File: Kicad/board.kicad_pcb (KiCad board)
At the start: 2 copper layers, 100 x 91.4 mm, 28 parts, among them SW1 SW_Push, SW10 SW_Push, SW11 SW_Push, SW12 SW_Push, SW13 RotaryEncoder, SW2 SW_Push, SW3 SW_Push, SW4 SW_Push, SW5 SW_Push, SW6 SW_Push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

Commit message: [add] add through hole
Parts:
- added H1: MountingHole, MountingHole:MountingHole_2.7mm, F.Cu at (62.9, 36.6)
- added H2: MountingHole, MountingHole:MountingHole_2.7mm, F.Cu at (154.9, 36.6)
- added H3: MountingHole, MountingHole:MountingHole_2.7mm, F.Cu at (62.9, 120.0)
- added H4: MountingHole, MountingHole:MountingHole_2.7mm, F.Cu at (154.9, 120.0)
- D1, D10, D11, D12, D2, D3, D4, D5, D6, D7, D8, D9: footprint Diode_SMD:D_SOD-323 -> mylib:1n4148ws_reversible
- moved U2 34.0 mm to (98.0, 107.7)
- moved U3 34.0 mm to (101.3, 122.0)
- moved SW13 21.7 mm to (145.9, 117.2)
- moved D2 14.2 mm to (94.3, 37.6)
- moved D1 14.2 mm to (75.3, 37.6)
- moved D3 14.2 mm to (113.4, 37.6)
- moved D4 14.2 mm to (132.4, 37.6)
- moved U1 3.03 mm to (146.7, 51.6)
- moved D5 2.37 mm to (64.9, 57.3)
- moved D6 2.37 mm to (82.9, 57.3)
- moved D7 2.37 mm to (100.9, 57.3)
- moved D8 2.37 mm to (118.9, 57.3)
- moved D10 2.32 mm to (83.7, 77.7)
- moved D11 2.32 mm to (100.7, 77.7)
- moved D12 2.32 mm to (117.7, 77.7)
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
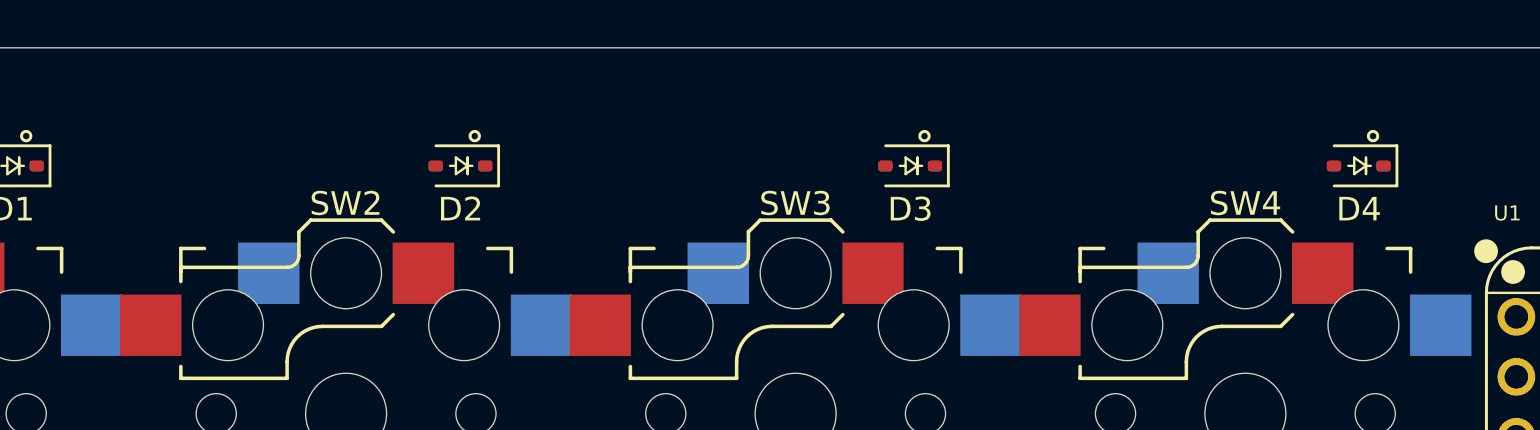
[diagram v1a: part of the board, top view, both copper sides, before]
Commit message: [update] move diodes
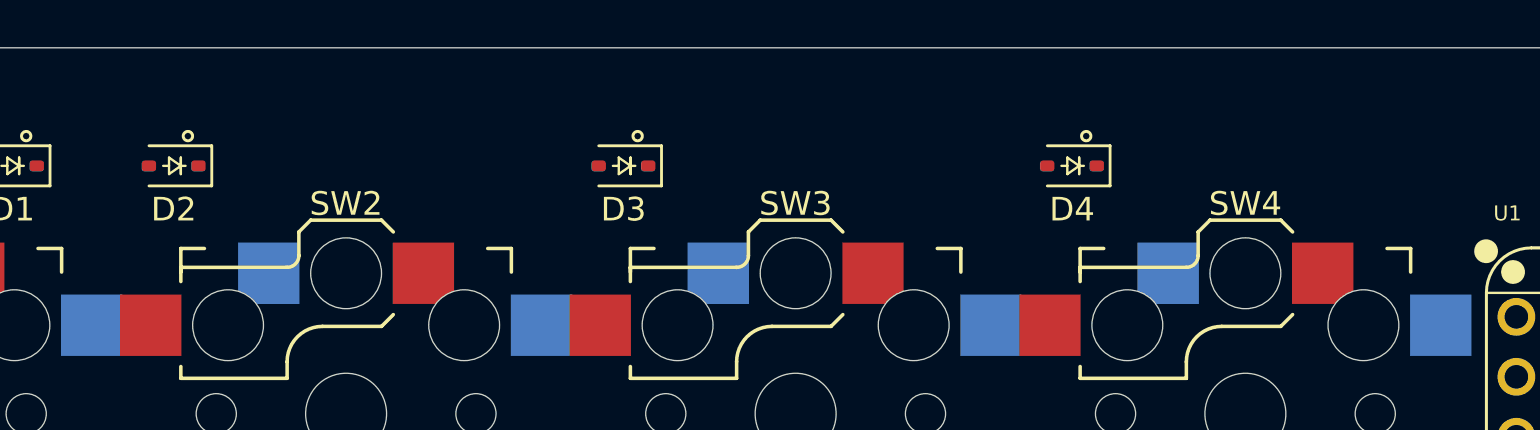
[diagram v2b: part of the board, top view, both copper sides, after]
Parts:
- moved D2 12.2 mm to (82.2, 37.6)
- moved D3 12.2 mm to (101.2, 37.6)
- moved D4 12.1 mm to (120.2, 37.6)
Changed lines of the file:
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@@
 	(footprint "mylib:1n4148ws_reversible"
 		(layer "F.Cu")
-		(at 113.3875 37.625 180)
+		(at 101.2375 37.625 180)
 		(descr "SOD-323")
 		(tags "SOD-323")
@@
 	(footprint "mylib:1n4148ws_reversible"
 		(layer "F.Cu")
-		(at 132.3875 37.625 180)
+		(at 120.2375 37.625 180)
 		(descr "SOD-323")
 		(tags "SOD-323")
@@
 	(footprint "mylib:1n4148ws_reversible"
 		(layer "F.Cu")
-		(at 94.3375 37.625 180)
+		(at 82.1875 37.625 180)
 		(descr "SOD-323")
 		(tags "SOD-323")

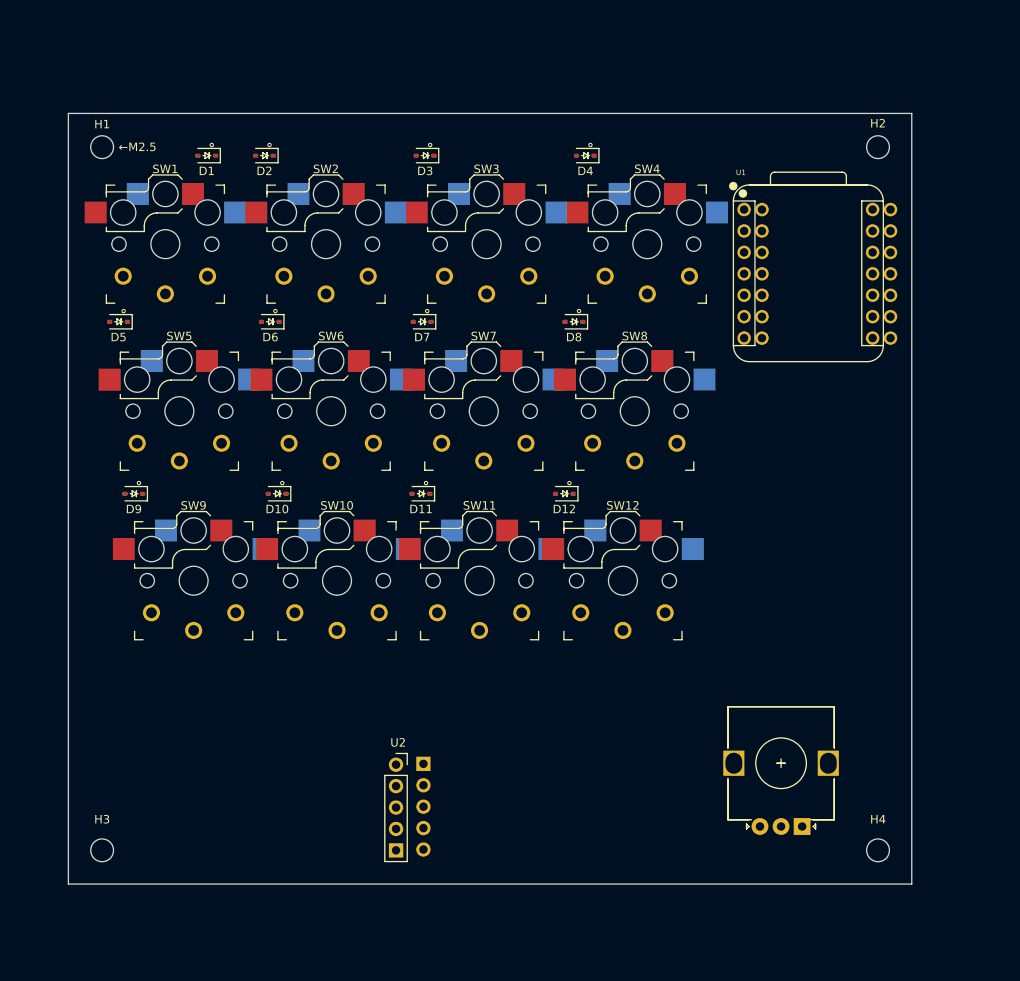
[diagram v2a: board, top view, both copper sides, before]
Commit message: [update] move key layout
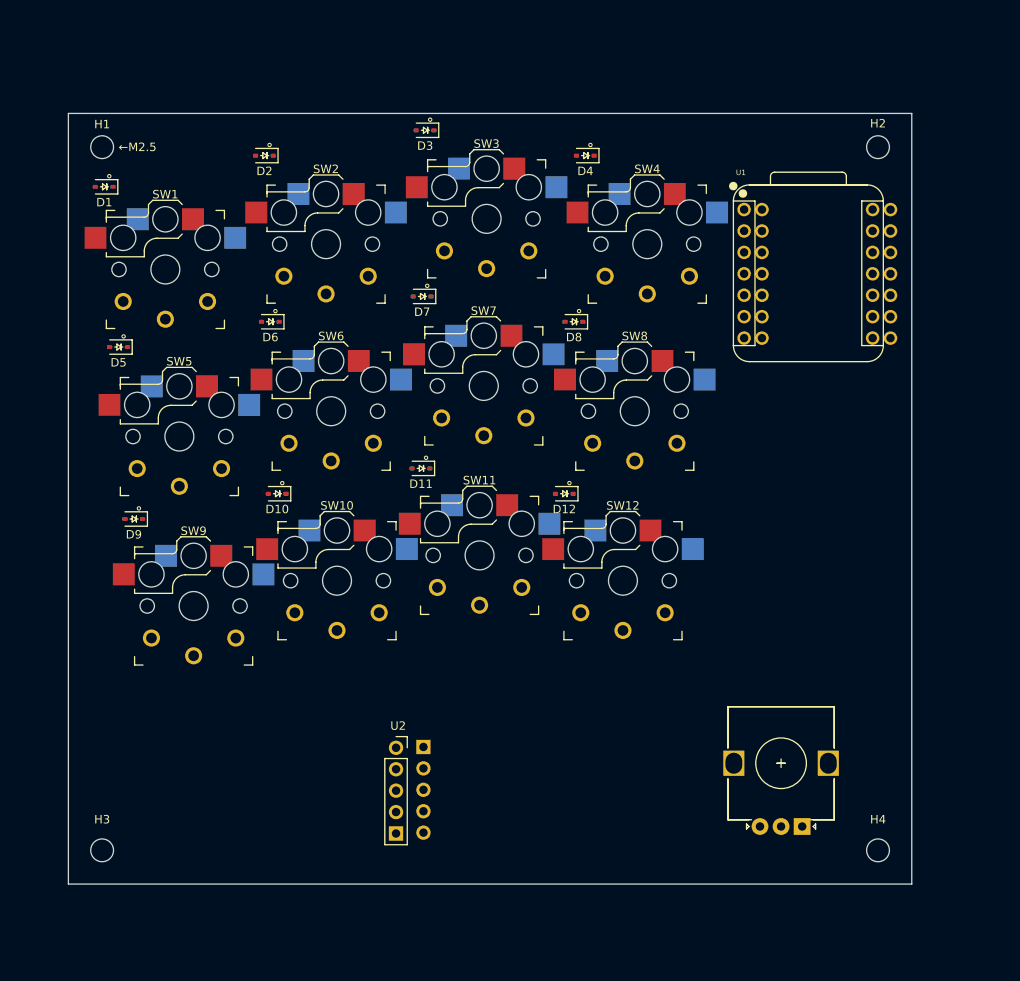
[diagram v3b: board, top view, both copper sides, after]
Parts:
- moved D1 12.7 mm to (63.2, 41.3)
- moved D11 3.00 mm to (100.7, 74.7)
- moved D3 3.00 mm to (101.2, 34.6)
- moved D5 3.00 mm to (64.9, 60.3)
- moved D7 3.00 mm to (100.9, 54.3)
- moved D9 3.00 mm to (66.7, 80.7)
- moved SW1 3.00 mm to (70.4, 51.1)
- moved SW11 3.00 mm to (107.7, 85.0)
- moved SW3 3.00 mm to (108.5, 45.1)
- moved SW5 3.00 mm to (72.1, 70.9)
- moved SW7 3.00 mm to (108.2, 64.9)
- moved SW9 3.00 mm to (73.8, 91.0)
- moved U2 2.00 mm to (98.0, 105.7)
- moved U3 2.00 mm to (101.3, 120.0)
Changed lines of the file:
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@@
 	(footprint "keyswitches:Kailh_socket_PG1350_optional_reversible"
 		(layer "F.Cu")
-		(at 72.0975 67.935)
+		(at 72.0975 70.935)
 		(descr "Kailh \"Choc\" PG1350 keyswitch with optional socket mount, reversible")
 		(tags "kailh,choc")
@@
 	(footprint "mylib:1n4148ws_reversible"
 		(layer "F.Cu")
-		(at 100.8875 57.325 180)
+		(at 100.8875 54.325 180)
 		(descr "SOD-323")
 		(tags "SOD-323")
@@
 	(footprint "keyswitches:Kailh_socket_PG1350_optional_reversible"
 		(layer "F.Cu")
-		(at 108.5285 48.125)
+		(at 108.5285 45.125)
 		(descr "Kailh \"Choc\" PG1350 keyswitch with optional socket mount, reversible")
 		(tags "kailh,choc")
@@
 	(footprint "mylib:1n4148ws_reversible"
 		(layer "F.Cu")
-		(at 100.7475 77.715 180)
+		(at 100.7475 74.715 180)
 		(descr "SOD-323")
 		(tags "SOD-323")
@@
 	(footprint "mylib:1n4148ws_reversible"
 		(layer "F.Cu")
-		(at 101.2375 37.625 180)
+		(at 101.2375 34.625 180)
 		(descr "SOD-323")
 		(tags "SOD-323")
@@
 	(footprint "mylib:1n4148ws_reversible"
 		(layer "F.Cu")
-		(at 66.6975 77.715 180)
+		(at 66.6975 80.715 180)
 		(descr "SOD-323")
 		(tags "SOD-323")
@@
 	(footprint "mylib:1n4148ws_reversible"
 		(layer "F.Cu")
-		(at 64.8875 57.325 180)
+		(at 64.8875 60.325 180)
 		(descr "SOD-323")
 		(tags "SOD-323")
@@
 	(footprint "keyswitches:Kailh_socket_PG1350_optional_reversible"
 		(layer "F.Cu")
-		(at 73.7875 88.03)
+		(at 73.7875 91.03)
 		(descr "Kailh \"Choc\" PG1350 keyswitch with optional socket mount, reversible")
 		(tags "kailh,choc")
@@
 	(footprint "keyswitches:Kailh_socket_PG1350_optional_reversible"
 		(layer "F.Cu")
-		(at 70.4375 48.125)
+		(at 70.4375 51.125)
 		(descr "Kailh \"Choc\" PG1350 keyswitch with optional socket mount, reversible")
 		(tags "kailh,choc")
@@
 	(footprint "mylib:1n4148ws_reversible"
 		(layer "F.Cu")
-		(at 75.3375 37.625 180)
+		(at 63.1875 41.325 180)
 		(descr "SOD-323")
 		(tags "SOD-323")
@@
 	(footprint "ky-023:KY-023"
 		(layer "F.Cu")
-		(at 98.0375 107.745)
+		(at 98.0375 105.745)
 		(property "Reference" "U2"
 			(at 0 -0.5 0)
@@
 	(footprint "keyswitches:Kailh_socket_PG1350_optional_reversible"
 		(layer "F.Cu")
-		(at 107.6925 88.03)
+		(at 107.6925 85.03)
 		(descr "Kailh \"Choc\" PG1350 keyswitch with optional socket mount, reversible")
 		(tags "kailh,choc")
@@
 	(footprint "keyswitches:Kailh_socket_PG1350_optional_reversible"
 		(layer "F.Cu")
-		(at 108.1925 67.935)
+		(at 108.1925 64.935)
 		(descr "Kailh \"Choc\" PG1350 keyswitch with optional socket mount, reversible")
 		(tags "kailh,choc")
@@
 	(footprint "ky-023:KY-023"
 		(layer "B.Cu")
-		(at 101.2875 122.005)
+		(at 101.2875 120.005)
 		(property "Reference" "U3"
 			(at 0 0.5 180)

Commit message: [update] routed
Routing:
- net column1: track 0.00 -> 175.8 mm, vias 0 -> 3
- net column2: track 0.00 -> 151.8 mm, vias 0 -> 3
- net GNDPWR: track 0.00 -> 145.8 mm
- net row3: track 0.00 -> 139.3 mm, vias 0 -> 5
- net column3: track 0.00 -> 138.5 mm, vias 0 -> 3
- net column4: track 0.00 -> 125.2 mm, vias 0 -> 1
- net VCC: track 0.00 -> 121.2 mm, vias 0 -> 1
- net joystick_x: track 0.00 -> 121.2 mm, vias 0 -> 1
- net joystick_y: track 0.00 -> 119.4 mm, vias 0 -> 1
- net row1: track 0.00 -> 117.7 mm, vias 0 -> 5
- net row2: track 0.00 -> 113.1 mm, vias 0 -> 5
- net rotary_encoder_b: track 0.00 -> 77.0 mm
- net rotary_encoder_a: track 0.00 -> 74.5 mm
- net Net-(D2-A): track 0.00 -> 51.8 mm
- net Net-(D8-A): track 0.00 -> 50.6 mm
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
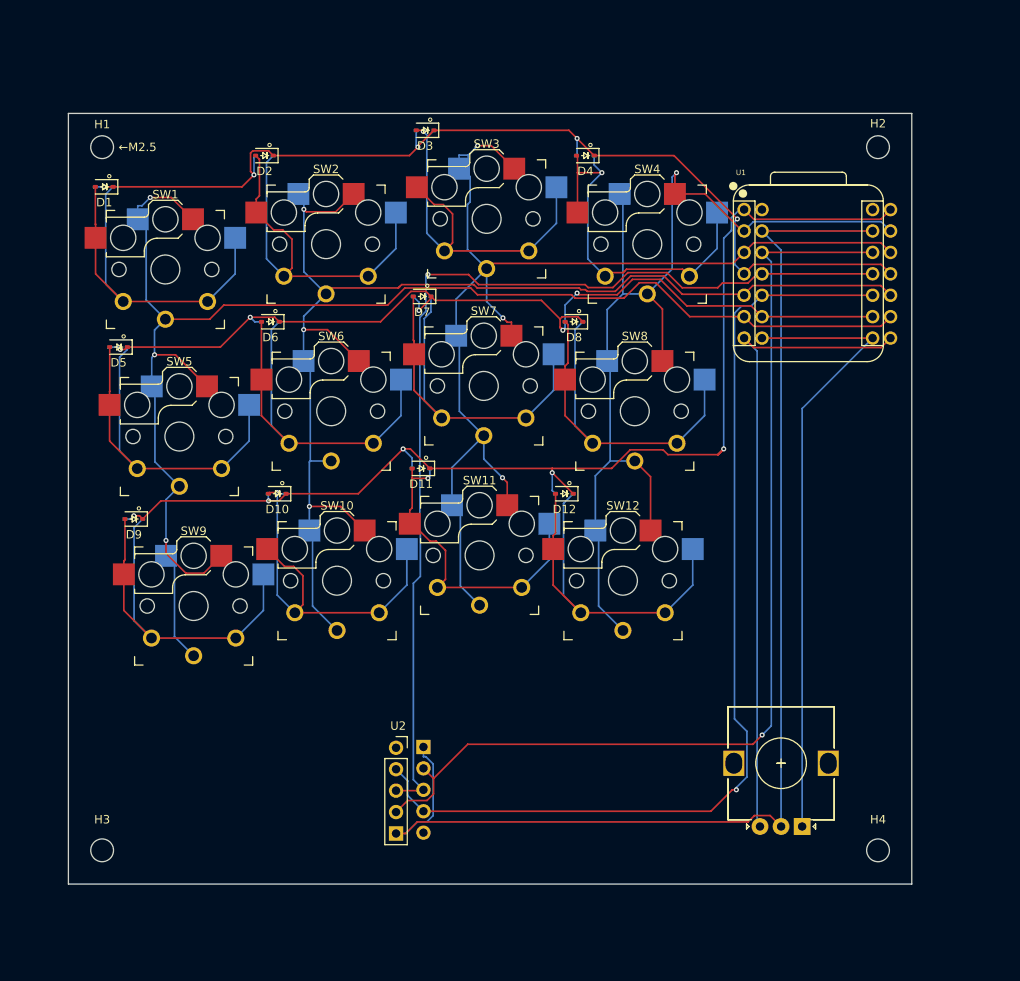
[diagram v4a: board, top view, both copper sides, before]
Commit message: [add] add sign to silk layer
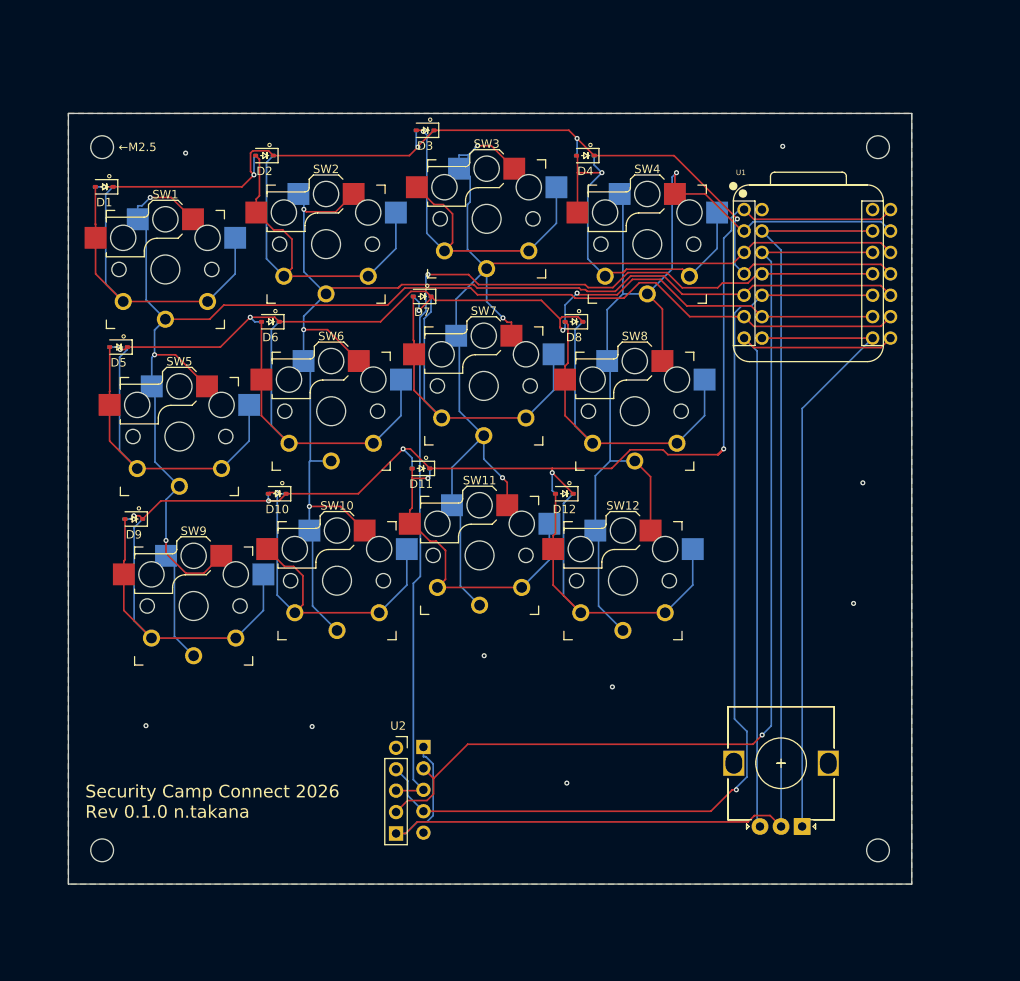
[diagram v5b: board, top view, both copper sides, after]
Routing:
- net GNDPWR: vias 0 -> 9
- added copper zone on B.Cu, net GNDPWR
- added copper zone on F.Cu, net GNDPWR
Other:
- board text added: "Security Camp Connect 2026 Rev 0.1.0 n.takana"
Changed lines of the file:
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@@
 			(at 0 -2.7 0)
 			(layer "F.SilkS")
+			(hide yes)
 			(effects
 				(font
@@
 			(at 0 -3.65 0)
 			(layer "F.SilkS")
+			(hide yes)
 			(effects
 				(font
@@
 			(at 0 -2.8 0)
 			(layer "F.SilkS")
+			(hide yes)
 			(effects
 				(font
@@
 			(at 0 -3.65 0)
 			(layer "F.SilkS")
+			(hide yes)
 			(effects
 				(font
@@
 		(layer "Edge.Cuts")
 	)
+	(gr_text "Security Camp Connect 2026\nRev 0.1.0 n.takana"
+		(at 60.9375 116.325 0)
+		(layer "F.SilkS")
+		(effects
+			(font
+				(size 1.5 1.5)
+				(thickness 0.2)
+			)
+			(justify left bottom)
+		)
+	)
+	(gr_text "Security Camp Connect 2026\nRev 0.1.0 n.takana"
+		(at 94.5375 116.325 -0)
+		(layer "B.SilkS")
+		(effects
+			(font
+				(size 1.5 1.5)
+				(thickness 0.2)
+			)
+			(justify left bottom mirror)
+		)
+	)
+	(dimension
+		(type orthogonal)
+		(layer "F.Fab")
+		(pts
+			(xy 58.9375 32.625) (xy 158.9375 32.625)
+		)
+		(height -5.2)
+		(orientation 0)
+		(format
+			(prefix "")
+			(suffix "")
+			(units 3)
+			(units_format 0)
+			(precision 4)
+			(suppress_zeroes yes)
+		)
+		(style
+			(thickness 0.1)
+			(arrow_length 1.27)
+			(text_position_mode 0)
+			(arrow_direction outward)
+			(extension_height 0.58642)
+			(extension_offset 0.5)
+			(keep_text_aligned yes)
+		)
+		(gr_text "100"
+			(at 108.9375 26.275 0)
+			(layer "F.Fab")
+			(effects
+				(font
+					(size 1 1)
+					(thickness 0.15)
+				)
+			)
+		)
+	)
+	(dimension
+		(type orthogonal)
+		(layer "F.Fab")
+		(pts
+			(xy 158.9375 32.625) (xy 158.9375 124.025)
+		)
+		(height 4.9)
+		(orientation 1)
+		(format
+			(prefix "")
+			(suffix "")
+			(units 3)
+			(units_format 0)
+			(precision 4)
+			(suppress_zeroes yes)
+		)
+		(style
+			(thickness 0.1)
+			(arrow_length 1.27)
+			(text_position_mode 0)
+			(arrow_direction outward)
+			(extension_height 0.58642)
+			(extension_offset 0.5)
+			(keep_text_aligned yes)
+		)
+		(gr_text "91.4"
+			(at 162.6875 78.325 90)
+			(layer "F.Fab")
+			(effects
+				(font
+					(size 1 1)
+					(thickness 0.15)
+				)
+			)
+		)
+	)
 	(segment
 		(start 100.3782 36.6167)
@@
 		(net 20)
 	)
+	(via
+		(at 153.1375 76.425)
+		(size 0.6)
+		(drill 0.3)
+		(layers "F.Cu" "B.Cu")
+		(free yes)
+		(net 20)
+	)
+	(via
+		(at 87.8375 105.325)
+		(size 0.6)
+		(drill 0.3)
+		(layers "F.Cu" "B.Cu")
+		(free yes)
+		(net 20)
+	)
+	(via
+		(at 123.4375 100.625)
+		(size 0.6)
+		(drill 0.3)
+		(layers "F.Cu" "B.Cu")
+		(free yes)
+		(net 20)
+	)
+	(via
+		(at 108.2375 96.925)
+		(size 0.6)
+		(drill 0.3)
+		(layers "F.Cu" "B.Cu")
+		(free yes)
+		(net 20)
+	)
+	(via
+		(at 118.0375 112.025)
+		(size 0.6)
+		(drill 0.3)
+		(layers "F.Cu" "B.Cu")
+		(free yes)
+		(net 20)
+	)
+	(via
+		(at 68.1375 105.225)
+		(size 0.6)
+		(drill 0.3)
+		(layers "F.Cu" "B.Cu")
+		(free yes)
+		(net 20)
+	)
+	(via
+		(at 72.8375 37.325)
+		(size 0.6)
+		(drill 0.3)
+		(layers "F.Cu" "B.Cu")
+		(free yes)
+		(net 20)
+	)
+	(via
+		(at 143.6375 36.525)
+		(size 0.6)
+		(drill 0.3)
+		(layers "F.Cu" "B.Cu")
+		(free yes)
+		(net 20)
+	)
+	(via
+		(at 152.0375 90.725)
+		(size 0.6)
+		(drill 0.3)
+		(layers "F.Cu" "B.Cu")
+		(free yes)
+		(net 20)
+	)
 	(segment
 		(start 98.9392 118.005)
@@
 		(net 26)
 	)
+	(zone
+		(net 20)
+		(net_name "GNDPWR")
+		(layer "F.Cu")
+		(hatch edge 0.5)
+		(connect_pads
+			(clearance 0.5)
+		)
+		(min_thickness 0.25)
+		(filled_areas_thickness no)
+		(fill yes
+			(thermal_gap 0.5)
+			(thermal_bridge_width 0.5)
+		)
+		(polygon
+			(pts
+				(xy 58.9375 32.625) (xy 158.9375 32.625) (xy 158.9375 124.025) (xy 58.9375 124.025)
+			)
+		)
+	)
+	(zone
+		(net 20)
+		(net_name "GNDPWR")
+		(layer "B.Cu")
+		(hatch edge 0.5)
+		(priority 1)
+		(connect_pads
+			(clearance 0.5)
+		)
+		(min_thickness 0.25)
+		(filled_areas_thickness no)
+		(fill yes
+			(thermal_gap 0.5)
+			(thermal_bridge_width 0.5)
+		)
+		(polygon
+			(pts
+				(xy 58.9375 32.625) (xy 158.9375 32.625) (xy 158.9375 124.025) (xy 58.9375 124.025)
+			)
+		)
+	)
 	(embedded_fonts no)
